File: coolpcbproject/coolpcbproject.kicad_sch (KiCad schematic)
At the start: 24 parts, among them SW1 SW_Push, U1 ATmega32U4-A, Y1 16 MHz

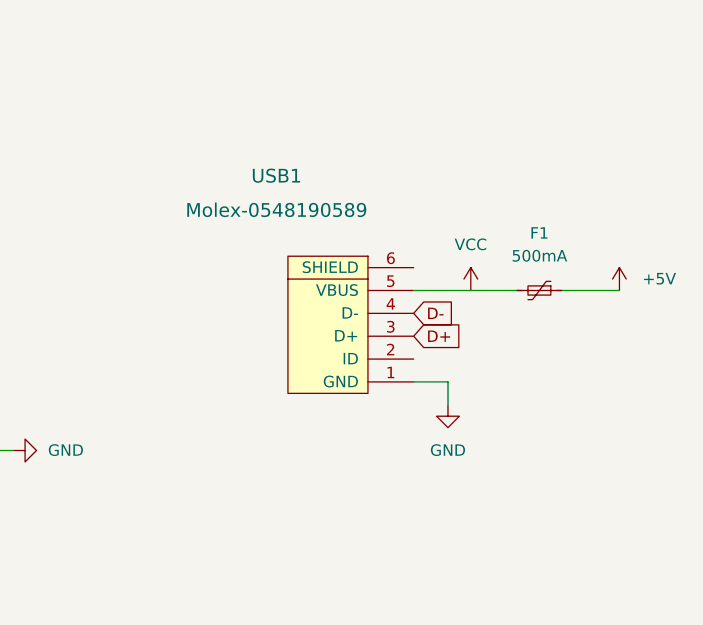
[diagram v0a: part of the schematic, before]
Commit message: adding usb c pretty
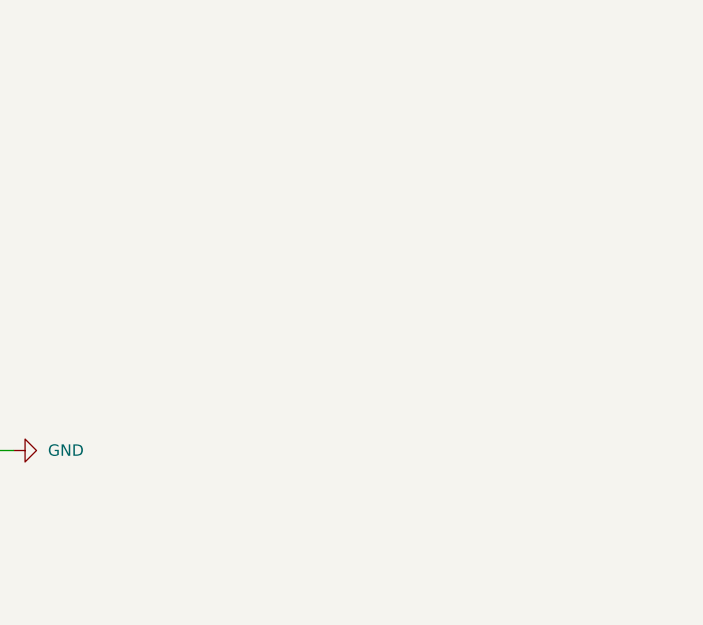
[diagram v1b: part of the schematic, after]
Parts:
- removed F1: 500mA, Fuse:Fuse_1206_3216Metric, symbol Device:Polyfuse_Small
- removed USB1: Molex-0548190589, symbol random-keyboard-parts:Molex-0548190589
- SW1: footprint (none) -> random-keyboard-parts:SKQG-1155865
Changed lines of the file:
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@@
-    (stroke (width 0) (type default) (color 0 0 0 0))
-  )
-  (wire (pts (xy 223.52 88.9) (xy 227.33 88.9))
-    (stroke (width 0) (type default) (color 0 0 0 0))
-  )
-  (wire (pts (xy 223.52 78.74) (xy 234.95 78.74))
     (stroke (width 0) (type default) (color 0 0 0 0))
   )
@@
     (stroke (width 0) (type default) (color 0 0 0 0))
   )
-  (wire (pts (xy 227.33 88.9) (xy 227.33 91.44))
-    (stroke (width 0) (type default) (color 0 0 0 0))
-  )
   (wire (pts (xy 111.76 76.2) (xy 115.57 76.2))
     (stroke (width 0) (type default) (color 0 0 0 0))
@@
   )
   (wire (pts (xy 144.78 35.56) (xy 147.32 35.56))
-    (stroke (width 0) (type default) (color 0 0 0 0))
-  )
-  (wire (pts (xy 240.03 78.74) (xy 246.38 78.74))
     (stroke (width 0) (type default) (color 0 0 0 0))
   )
@@
     )
   )
-  (global_label "D+" (shape input) (at 223.52 83.82 0) (fields_autoplaced)
-    (effects (font (size 1.27 1.27)) (justify left))
-    (property "Intersheet References" "${INTERSHEET_REFS}" (id 0) (at 228.7755 83.8994 0)
-      (effects (font (size 1.27 1.27)) (justify left) hide)
-    )
-  )
-  (global_label "D-" (shape input) (at 223.52 81.28 0) (fields_autoplaced)
-    (effects (font (size 1.27 1.27)) (justify left))
-    (property "Intersheet References" "${INTERSHEET_REFS}" (id 0) (at 228.7755 81.3594 0)
-      (effects (font (size 1.27 1.27)) (justify left) hide)
-    )
-  )
   (symbol (lib_id "power:+5V") (at 118.11 63.5 0) (unit 1)
     (in_bom yes) (on_board yes)
@@
     )
     (property "Datasheet" "" (id 3) (at 118.11 63.5 0)
-      (effects (font (size 1.27 1.27)) hide)
-    )
-    (pin "1")
-  )
-  (symbol (lib_id "power:VCC") (at 229.87 78.74 0) (unit 1)
-    (in_bom yes) (on_board yes) (fields_autoplaced)
-    (property "Reference" "#PWR0110" (id 0) (at 229.87 82.55 0)
-      (effects (font (size 1.27 1.27)) hide)
-    )
-    (property "Value" "VCC" (id 1) (at 229.87 73.66 0))
-    (property "Footprint" "" (id 2) (at 229.87 78.74 0)
-      (effects (font (size 1.27 1.27)) hide)
-    )
-    (property "Datasheet" "" (id 3) (at 229.87 78.74 0)
       (effects (font (size 1.27 1.27)) hide)
     )
@@
     (pin "2")
   )
-  (symbol (lib_id "power:+5V") (at 246.38 78.74 0) (unit 1)
-    (in_bom yes) (on_board yes) (fields_autoplaced)
-    (property "Reference" "#PWR0109" (id 0) (at 246.38 82.55 0)
-      (effects (font (size 1.27 1.27)) hide)
-    )
-    (property "Value" "+5V" (id 1) (at 248.92 77.4699 0)
-      (effects (font (size 1.27 1.27)) (justify left))
-    )
-    (property "Footprint" "" (id 2) (at 246.38 78.74 0)
-      (effects (font (size 1.27 1.27)) hide)
-    )
-    (property "Datasheet" "" (id 3) (at 246.38 78.74 0)
-      (effects (font (size 1.27 1.27)) hide)
-    )
-    (pin "1")
-  )
   (symbol (lib_id "Device:Crystal_GND24_Small") (at 115.57 50.8 90) (unit 1)
     (in_bom yes) (on_board yes)
@@
     (pin "1")
   )
-  (symbol (lib_id "random-keyboard-parts:Molex-0548190589") (at 215.9 83.82 90) (unit 1)
-    (in_bom yes) (on_board yes)
-    (property "Reference" "USB1" (id 0) (at 208.28 66.04 90)
-      (effects (font (size 1.524 1.524)))
-    )
-    (property "Value" "Molex-0548190589" (id 1) (at 208.28 69.85 90)
-      (effects (font (size 1.524 1.524)))
-    )
-    (property "Footprint" "" (id 2) (at 215.9 83.82 0)
-      (effects (font (size 1.524 1.524)) hide)
-    )
-    (property "Datasheet" "" (id 3) (at 215.9 83.82 0)
-      (effects (font (size 1.524 1.524)) hide)
-    )
-    (pin "1")
-    (pin "2")
-    (pin "3")
-    (pin "4")
-    (pin "5")
-    (pin "6")
-  )
   (symbol (lib_id "MX_Alps_Hybrid:MX-NoLED") (at 57.15 167.64 0) (unit 1)
     (in_bom yes) (on_board yes) (fields_autoplaced)
@@
     )
     (property "Datasheet" "" (id 3) (at 101.6 87.63 0)
-      (effects (font (size 1.27 1.27)) hide)
-    )
-    (pin "1")
-  )
-  (symbol (lib_id "power:GND") (at 227.33 91.44 0) (unit 1)
-    (in_bom yes) (on_board yes) (fields_autoplaced)
-    (property "Reference" "#PWR0111" (id 0) (at 227.33 97.79 0)
-      (effects (font (size 1.27 1.27)) hide)
-    )
-    (property "Value" "GND" (id 1) (at 227.33 96.52 0))
-    (property "Footprint" "" (id 2) (at 227.33 91.44 0)
-      (effects (font (size 1.27 1.27)) hide)
-    )
-    (property "Datasheet" "" (id 3) (at 227.33 91.44 0)
       (effects (font (size 1.27 1.27)) hide)
     )
@@
     (pin "2")
   )
-  (symbol (lib_id "Device:Polyfuse_Small") (at 237.49 78.74 270) (unit 1)
-    (in_bom yes) (on_board yes) (fields_autoplaced)
-    (property "Reference" "F1" (id 0) (at 237.49 72.39 90))
-    (property "Value" "500mA" (id 1) (at 237.49 74.93 90))
-    (property "Footprint" "Fuse:Fuse_1206_3216Metric" (id 2) (at 232.41 80.01 0)
-      (effects (font (size 1.27 1.27)) (justify left) hide)
-    )
-    (property "Datasheet" "~" (id 3) (at 237.49 78.74 0)
-      (effects (font (size 1.27 1.27)) hide)
-    )
-    (pin "1")
-    (pin "2")
-  )
   (symbol (lib_id "power:+5V") (at 142.24 27.94 0) (unit 1)
     (in_bom yes) (on_board yes) (fields_autoplaced)
@@
     (property "Reference" "SW1" (id 0) (at 114.3 27.94 0))
     (property "Value" "SW_Push" (id 1) (at 114.3 30.48 0))
-    (property "Footprint" "" (id 2) (at 114.3 30.48 0)
+    (property "Footprint" "random-keyboard-parts:SKQG-1155865" (id 2) (at 114.3 30.48 0)
       (effects (font (size 1.27 1.27)) hide)
     )
@@
       (reference "#PWR0108") (unit 1) (value "GND") (footprint "")
     )
-    (path "/1c70229b-c444-4fb4-a3fb-d9964aeadb84"
-      (reference "#PWR0109") (unit 1) (value "+5V") (footprint "")
-    )
-    (path "/09c9b035-d615-4ea0-8ae6-930406cb108f"
-      (reference "#PWR0110") (unit 1) (value "VCC") (footprint "")
-    )
-    (path "/ad2d59d6-38a8-42a5-ace7-58476a14b2ae"
-      (reference "#PWR0111") (unit 1) (value "GND") (footprint "")
-    )
     (path "/f58484d1-7253-421e-b465-b0bcf9a7ca79"
       (reference "#PWR0112") (unit 1) (value "GND") (footprint "")
@@
       (reference "D4") (unit 1) (value "D_Small") (footprint "Diode_SMD:D_SOD-123")
     )
-    (path "/e13ba972-2c92-44aa-9932-ecfd4d5d552a"
-      (reference "F1") (unit 1) (value "500mA") (footprint "Fuse:Fuse_1206_3216Metric")
-    )
     (path "/d526f494-296d-4f6a-b51b-928c7cff98d2"
       (reference "MX1") (unit 1) (value "MX-NoLED") (footprint "MX_Alps_Hybrid:MX-1U-NoLED")
@@
     )
     (path "/ebcd0372-7455-4405-93e9-b24e6f7c00e3"
-      (reference "SW1") (unit 1) (value "SW_Push") (footprint "")
+      (reference "SW1") (unit 1) (value "SW_Push") (footprint "random-keyboard-parts:SKQG-1155865")
     )
     (path "/d49e4fd2-44d0-4d76-9f57-1e6c160dfe14"
       (reference "U1") (unit 1) (value "ATmega32U4-A") (footprint "Package_QFP:TQFP-44_10x10mm_P0.8mm")
     )
-    (path "/95162d3b-9855-4b95-a640-b70221507d4b"
-      (reference "USB1") (unit 1) (value "Molex-0548190589") (footprint "")
-    )
     (path "/21c2ac49-9695-4a3e-9676-0cff677df983"

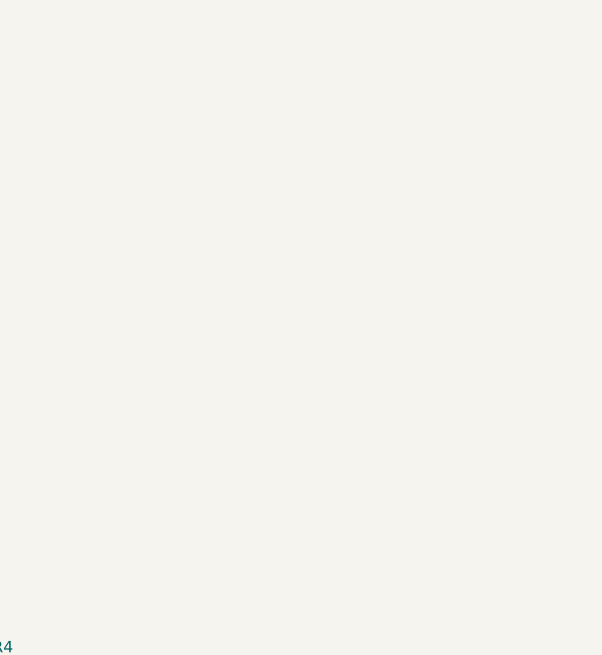
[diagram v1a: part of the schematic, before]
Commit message: libraries and usb c fix
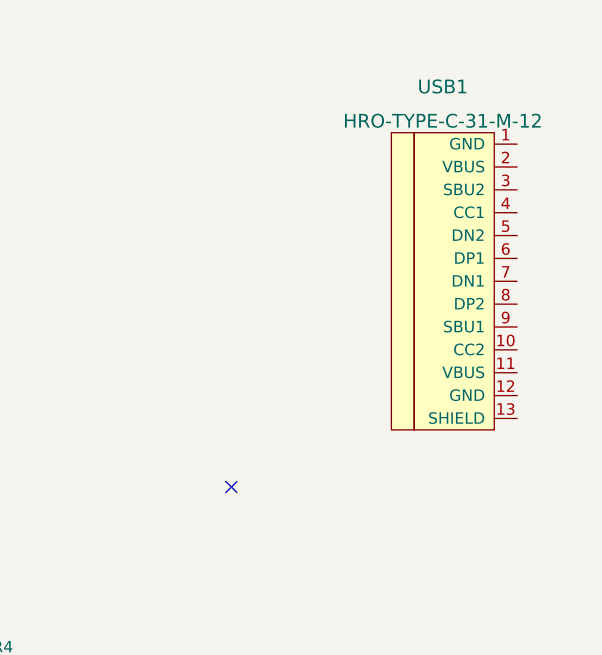
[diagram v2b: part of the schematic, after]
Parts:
- added USB1: HRO-TYPE-C-31-M-12, Type-C:HRO-TYPE-C-31-M-12-Assembly, symbol Type-C:HRO-TYPE-C-31-M-12
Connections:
- no-connect marks 4 -> 5
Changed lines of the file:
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@@
   (no_connect (at 38.1 149.86))
   (no_connect (at 58.42 173.99))
+  (no_connect (at 195.58 72.39))
   (no_connect (at 58.42 149.86))
   (no_connect (at 38.1 173.99))
@@
     )
     (pin "1")
+  )
+  (symbol (lib_id "Type-C:HRO-TYPE-C-31-M-12") (at 224.79 48.26 0) (unit 1)
+    (in_bom yes) (on_board yes) (fields_autoplaced)
+    (property "Reference" "USB1" (id 0) (at 219.075 27.94 0)
+      (effects (font (size 1.524 1.524)))
+    )
+    (property "Value" "HRO-TYPE-C-31-M-12" (id 1) (at 219.075 31.75 0)
+      (effects (font (size 1.524 1.524)))
+    )
+    (property "Footprint" "Type-C:HRO-TYPE-C-31-M-12-Assembly" (id 2) (at 224.79 48.26 0)
+      (effects (font (size 1.524 1.524)) hide)
+    )
+    (property "Datasheet" "" (id 3) (at 224.79 48.26 0)
+      (effects (font (size 1.524 1.524)) hide)
+    )
+    (pin "1")
+    (pin "10")
+    (pin "11")
+    (pin "12")
+    (pin "13")
+    (pin "2")
+    (pin "3")
+    (pin "4")
+    (pin "5")
+    (pin "6")
+    (pin "7")
+    (pin "8")
+    (pin "9")
   )
   (symbol (lib_id "Device:D_Small") (at 34.29 152.4 90) (unit 1)
@@
       (reference "U1") (unit 1) (value "ATmega32U4-A") (footprint "Package_QFP:TQFP-44_10x10mm_P0.8mm")
     )
+    (path "/b48d1d2b-1ef5-4a89-bdd4-95dbc90f4b6d"
+      (reference "USB1") (unit 1) (value "HRO-TYPE-C-31-M-12") (footprint "Type-C:HRO-TYPE-C-31-M-12-Assembly")
+    )
     (path "/21c2ac49-9695-4a3e-9676-0cff677df983"
